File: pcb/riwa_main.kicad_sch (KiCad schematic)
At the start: 19 parts, among them IC1 RV-3028-C7, J1 USB4105-GF-A, U1 DPS368XTSA1, U2 MS88SF2, U3 MCP73831/OT, U4 AP2112K-3.3

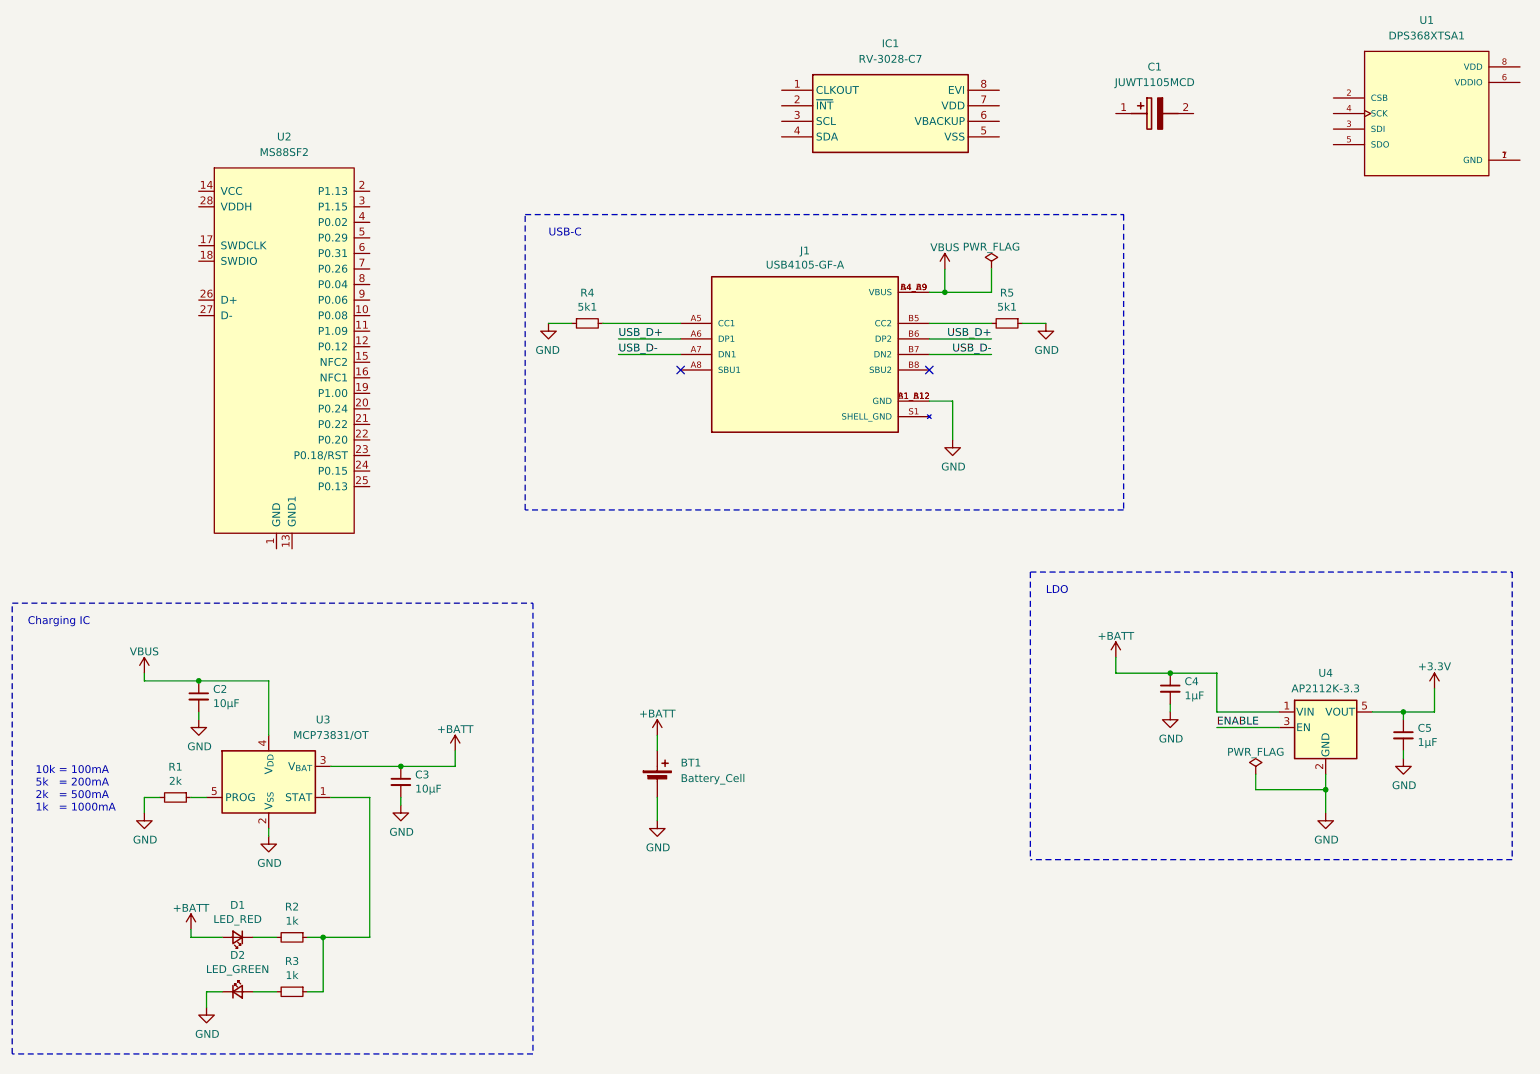
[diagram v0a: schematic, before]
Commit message: Placed components on PCB Board (no layouting)
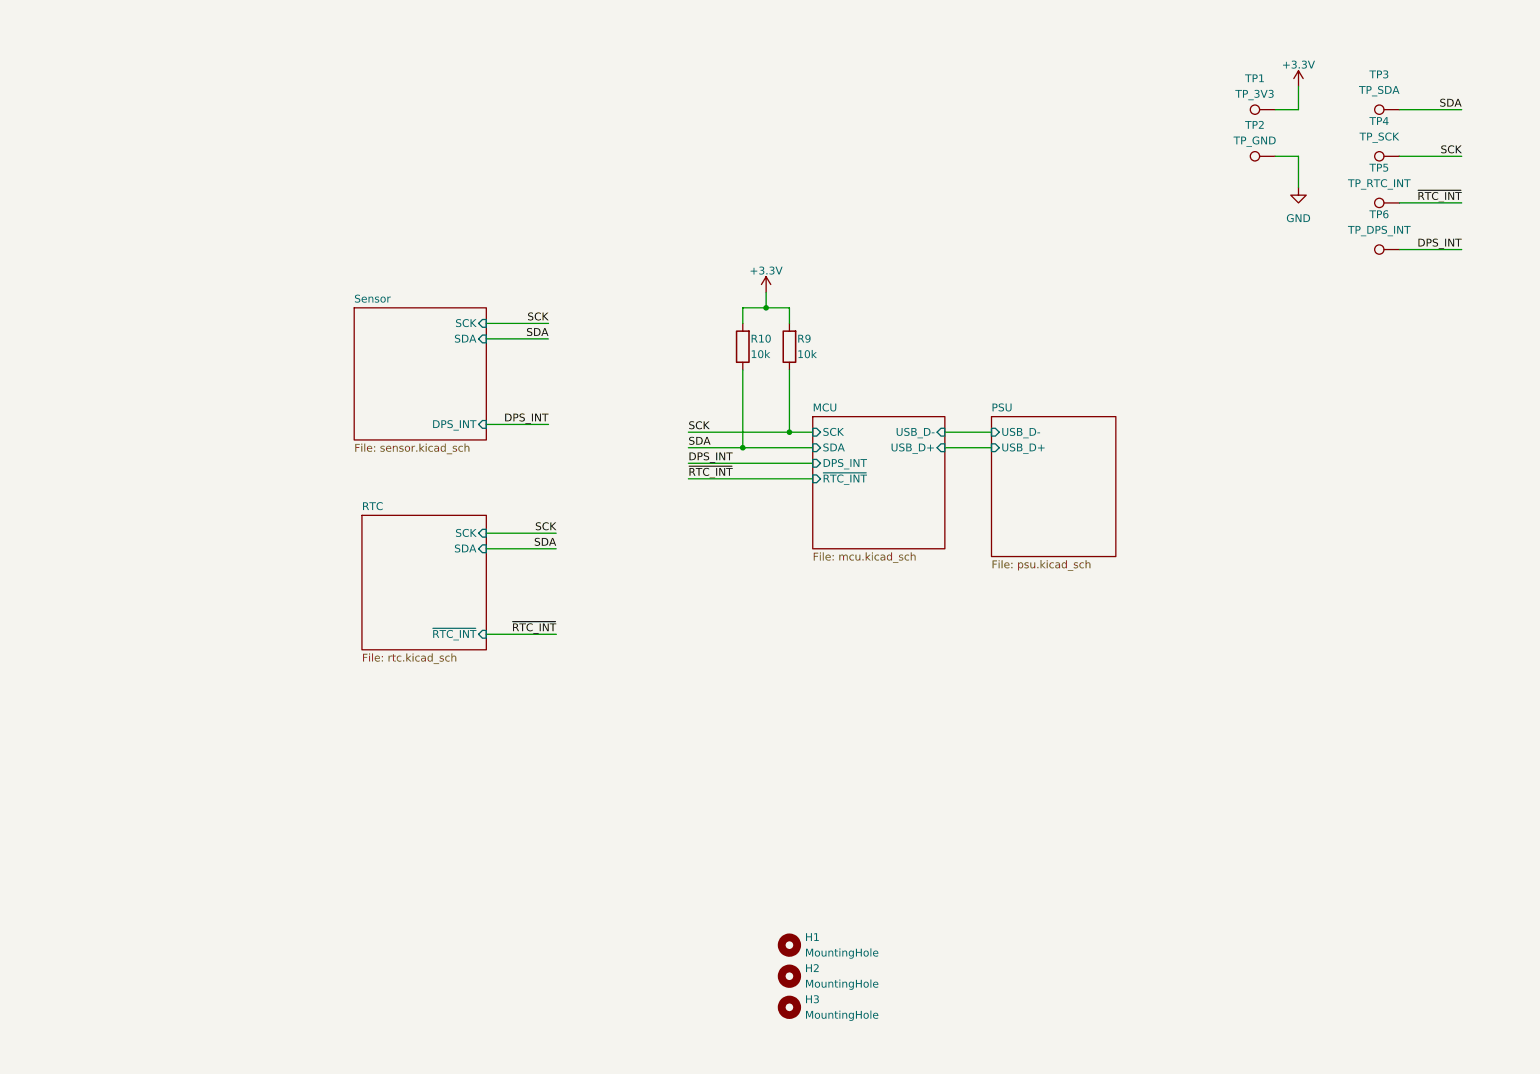
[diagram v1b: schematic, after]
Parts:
- removed BT1: Battery_Cell, Connector_JST:JST_PH_S2B-PH-SM4-TB_1x02-1MP_P2.00mm_Horizontal, symbol Device:Battery_Cell
- removed C1: JUWT1105MCD, JUWT1105MCD:CAPPRD250W50D655H1050, symbol JUWT1105MCD:JUWT1105MCD
- removed C2, C3: 10µF, Capacitor_SMD:C_0603_1608Metric, symbol Device:C_Small
- removed C4, C5: 1µF, Capacitor_SMD:C_0603_1608Metric, symbol Device:C_Small
- removed D1: LED_RED, LED_SMD:LED_0603_1608Metric, symbol Device:LED_Small
- removed D2: LED_GREEN, LED_SMD:LED_0603_1608Metric, symbol Device:LED_Small
- removed IC1: RV-3028-C7, RV-3028-C7:RV3028C732768kHz1ppmTAQC, symbol RV-3028-C7:RV-3028-C7
- removed J1: USB4105-GF-A, USB4105-GF-A:GCT_USB4105-GF-A, symbol USB4105-GF-A:USB4105-GF-A
- removed R1: 2k, Resistor_SMD:R_0603_1608Metric, symbol Device:R_Small
- removed R2, R3: 1k, Resistor_SMD:R_0603_1608Metric, symbol Device:R_Small
- removed R4, R5: 5k1, Resistor_SMD:R_0603_1608Metric, symbol Device:R_Small
- removed U1: DPS368XTSA1, DPS368XTSA1:XDCR_DPS368XTSA1, symbol DPS368XTSA1:DPS368XTSA1
- removed U2: MS88SF2, MS88SF2:MS88SF2, symbol MS88SF2:MS88SF2
- removed U3: MCP73831/OT, Package_TO_SOT_SMD:SOT-23-5, symbol Battery_Management:MCP73831-2-OT
- removed U4: AP2112K-3.3, Package_TO_SOT_SMD:SOT-23-5, symbol Regulator_Linear:AP2112K-3.3
- added H1, H2, H3: MountingHole, MountingHole:MountingHole_2.5mm, symbol Mechanical:MountingHole
- added R10, R9: 10k, Resistor_SMD:R_0603_1608Metric, symbol Device:R
- added TP1: TP_3V3, TestPoint:TestPoint_Pad_D2.0mm, symbol Connector:TestPoint
- added TP2: TP_GND, TestPoint:TestPoint_Pad_D2.0mm, symbol Connector:TestPoint
- added TP3: TP_SDA, TestPoint:TestPoint_Pad_D2.0mm, symbol Connector:TestPoint
- added TP4: TP_SCK, TestPoint:TestPoint_Pad_D2.0mm, symbol Connector:TestPoint
- added TP5: TP_RTC_INT, TestPoint:TestPoint_Pad_D2.0mm, symbol Connector:TestPoint
- added TP6: TP_DPS_INT, TestPoint:TestPoint_Pad_D2.0mm, symbol Connector:TestPoint
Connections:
- net +3.3V: now also R10.2, R9.2, TP1.1
- net GND: now also TP2.1
- new net DPS_INT: TP6.1
- new net SCK: R9.1, TP4.1
- new net SDA: R10.1, TP3.1
- new net ~{RTC_INT}: TP5.1
- no-connect marks 2 -> 0
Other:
- added sheet MCU (mcu.kicad_sch)
- added sheet PSU (psu.kicad_sch)
- added sheet RTC (rtc.kicad_sch)
- added sheet Sensor (sensor.kicad_sch)
- note removed: "10k = 100mA 5k = 200mA 2k = 500mA 1k = 1000mA"
- note removed: "Charging IC"
- note removed: "LDO"
- note removed: "USB-C"
- company: (none) -> OPEN THINGS
- title: (none) -> Openthing 3 River Watch

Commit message: Replaces nRF52840 with ESP32-S3
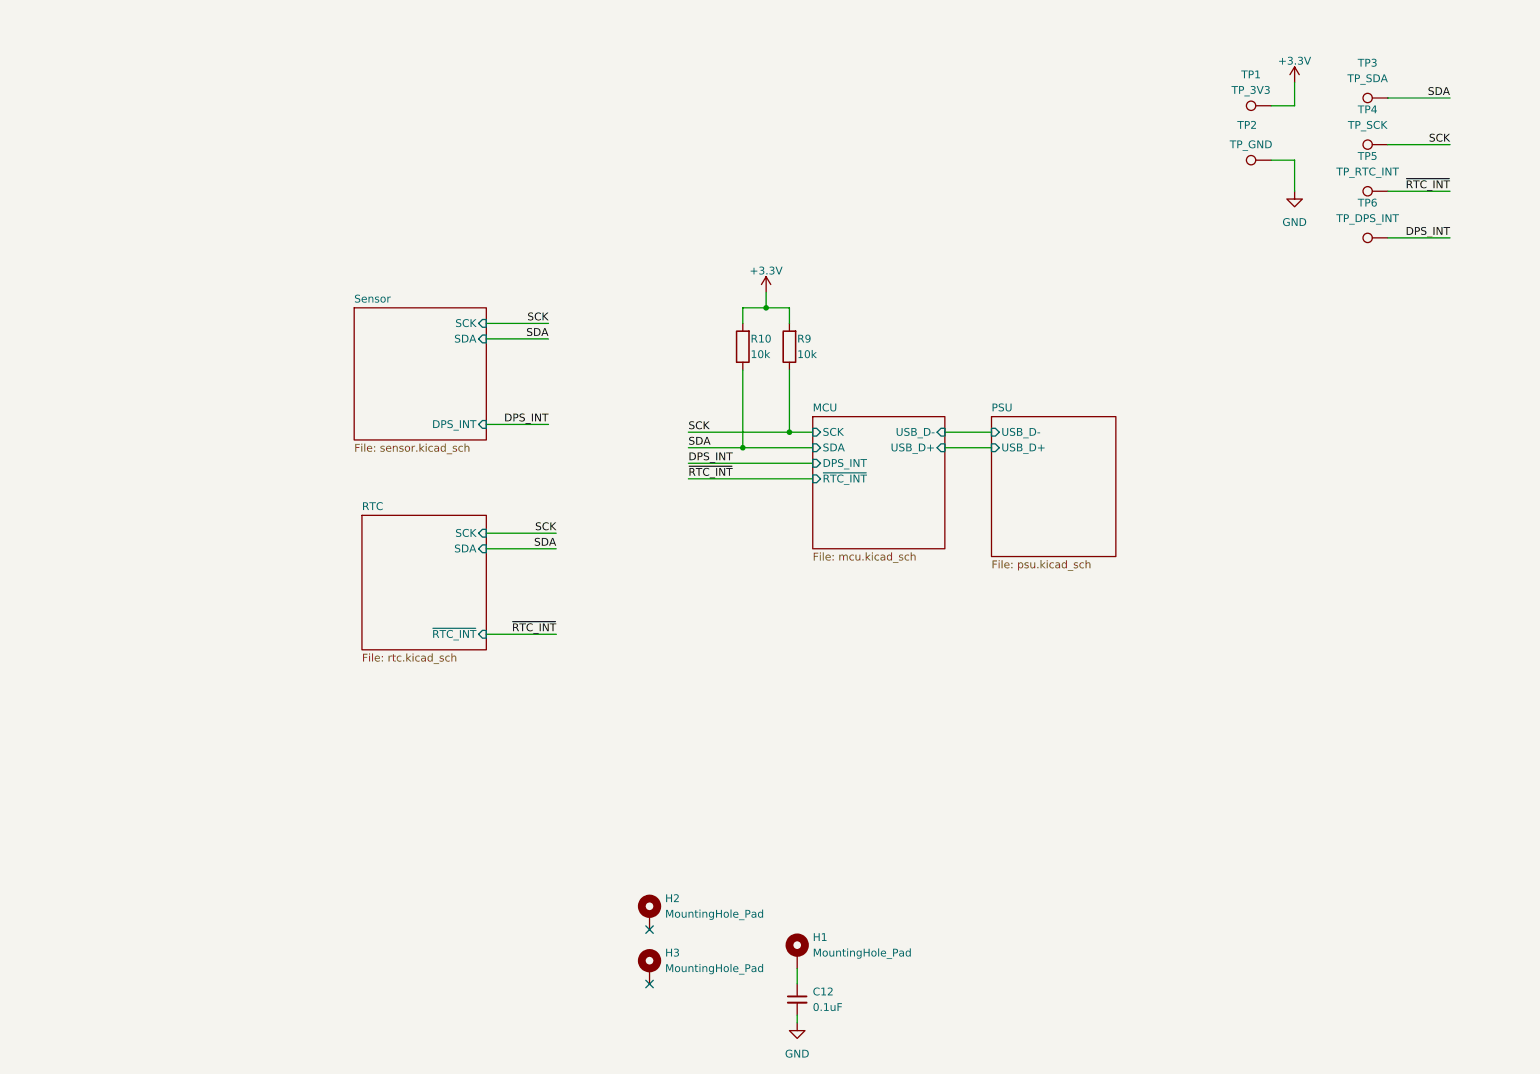
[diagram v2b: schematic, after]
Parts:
- removed H1, H2, H3: MountingHole, MountingHole:MountingHole_2.5mm, symbol Mechanical:MountingHole
- added C12: 0.1uF, Capacitor_SMD:C_0603_1608Metric, symbol Device:C_Small
- added H1, H2, H3: MountingHole_Pad, MountingHole:MountingHole_2.5mm_Pad_Via, symbol Mechanical:MountingHole_Pad
- TP1, TP2, TP3, TP4, TP5, TP6: footprint TestPoint:TestPoint_Pad_D2.0mm -> TestPoint:TestPoint_Pad_D1.5mm
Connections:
- net GND: now also C12.2
- new net: C12.1, H1.1
- no-connect marks 0 -> 2
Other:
- moved on the sheet: TP1, TP2, TP3, TP4, TP5, TP6

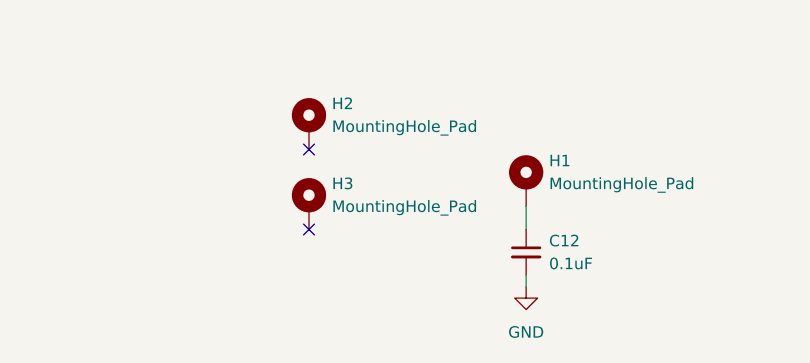
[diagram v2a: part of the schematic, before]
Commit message: Layout all components
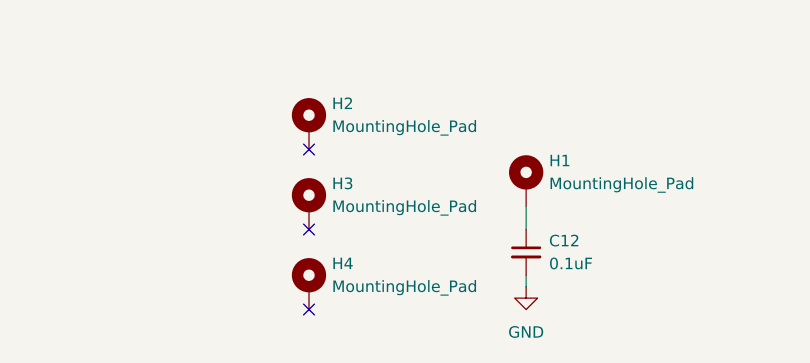
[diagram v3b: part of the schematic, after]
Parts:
- added H4: MountingHole_Pad, MountingHole:MountingHole_2.5mm_Pad_Via, symbol Mechanical:MountingHole_Pad
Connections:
- no-connect marks 2 -> 3
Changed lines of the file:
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@@
   (junction (at 146.05 91.44) (diameter 0) (color 0 0 0 0)
   )
+  (no_connect (at 130.81 187.96))
   (no_connect (at 130.81 179.07))
   (no_connect (at 130.81 170.18))
@@
         )
       )
+    )
+  )
+  (symbol (lib_id "Mechanical:MountingHole_Pad") (at 130.81 185.42 0) (unit 1)
+    (in_bom yes) (on_board yes) (dnp no) (fields_autoplaced)
+    (property "Reference" "H4" (at 133.35 182.88 0)
+      (effects (font (size 1.27 1.27)) (justify left))
+    )
+    (property "Value" "MountingHole_Pad" (at 133.35 185.42 0)
+      (effects (font (size 1.27 1.27)) (justify left))
+    )
+    (property "Footprint" "MountingHole:MountingHole_2.5mm_Pad_Via" (at 130.81 185.42 0)
+      (effects (font (size 1.27 1.27)) hide)
+    )
+    (property "Datasheet" "~" (at 130.81 185.42 0)
+      (effects (font (size 1.27 1.27)) hide)
+    )
+    (pin "1")
+    (instances
+      (project "ot-riwa"
+        (path "/27c79cfd-7e0d-4d78-9eed-2a8b043fdd67/56041fc6-6e17-4b0b-abcc-5d5fefb6b277"
+          (reference "H4") (unit 1)
+        )
+      )
